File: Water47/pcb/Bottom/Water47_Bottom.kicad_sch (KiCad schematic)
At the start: 5 parts, among them U1 MOUDLE-SEEEDUINO-XIAO

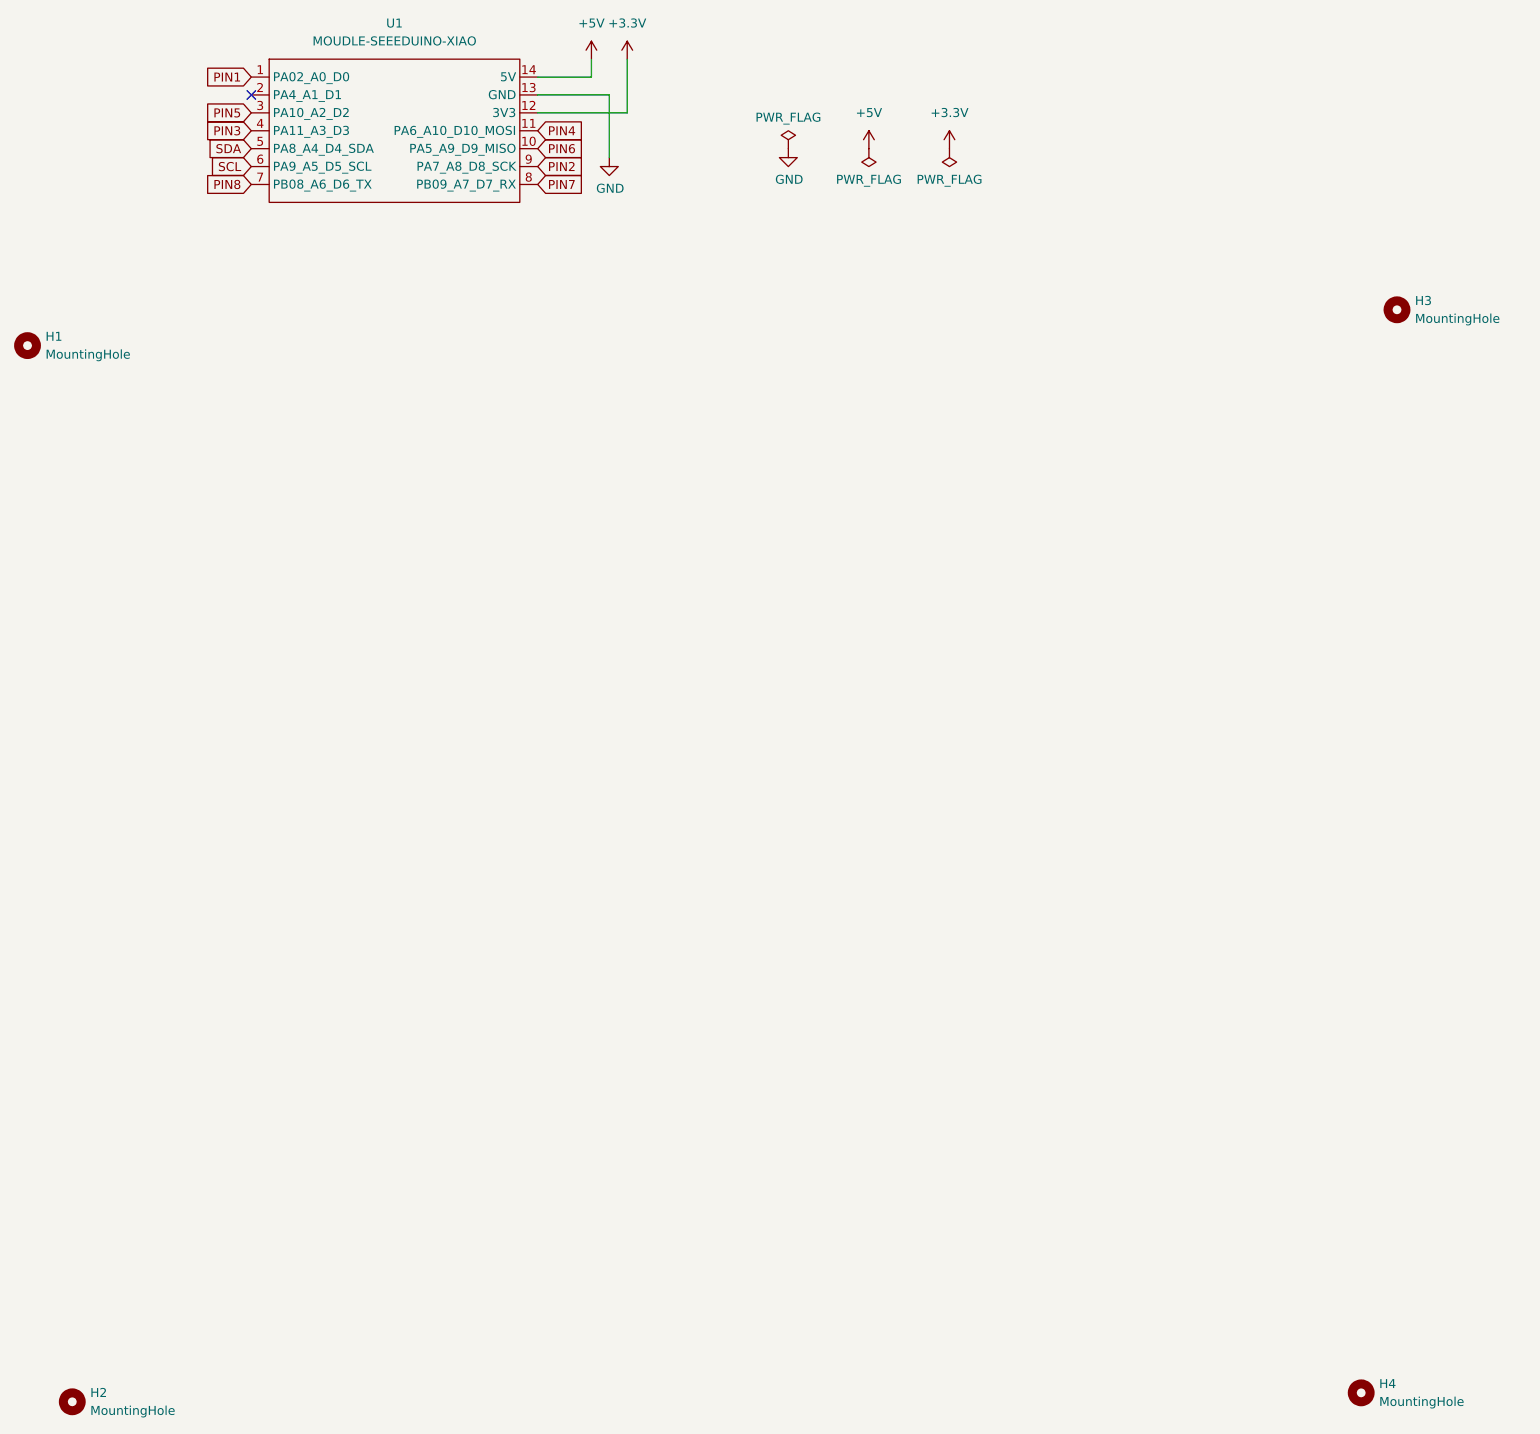
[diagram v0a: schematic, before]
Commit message: feat: add mounting holes
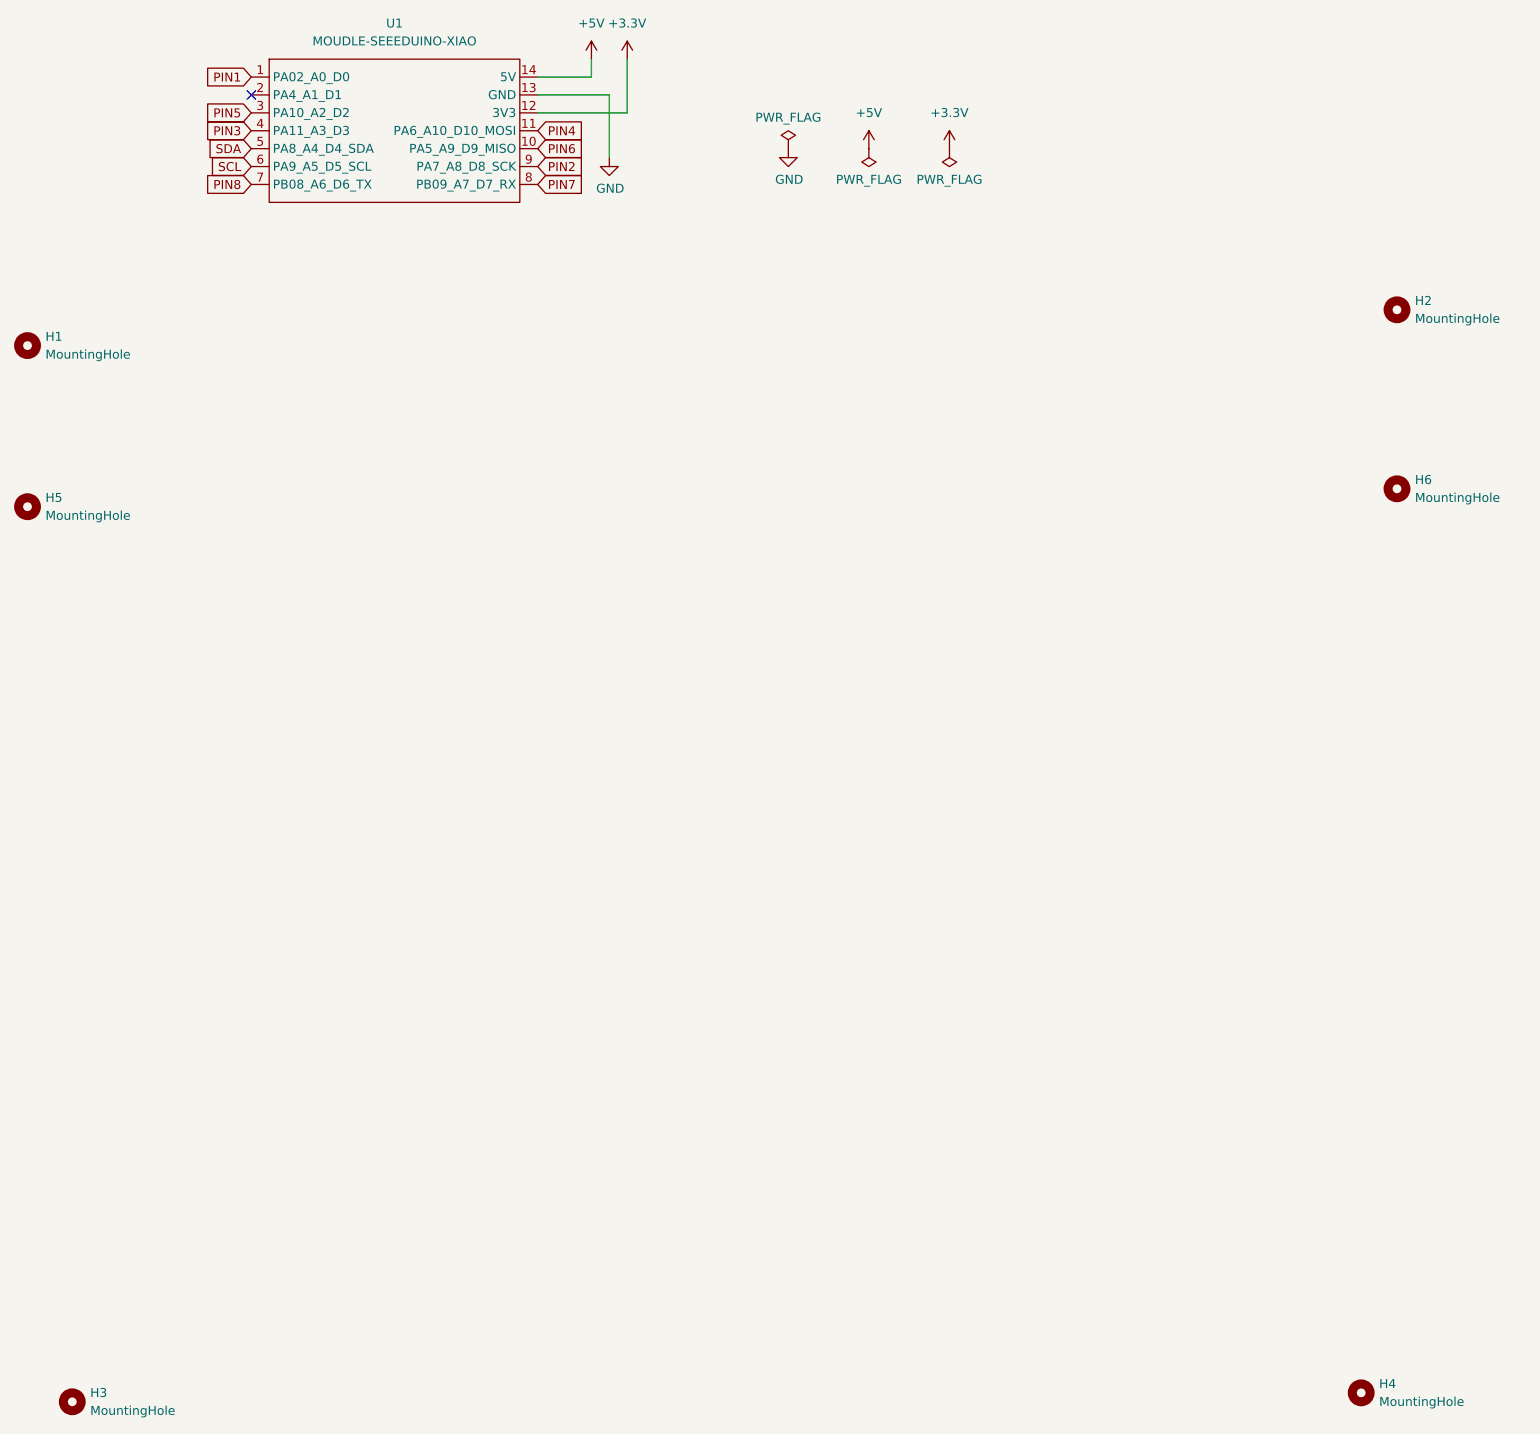
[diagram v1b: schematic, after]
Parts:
- added H5, H6: MountingHole, kbd_Hole:m2_Screw_Hole, symbol Mechanical:MountingHole
- renumbered H3 to H2, H2 to H3
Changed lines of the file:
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@@
+    )
+  )
+  (symbol (lib_id "Mechanical:MountingHole") (at 22.86 91.44 0) (unit 1)
+    (in_bom yes) (on_board yes) (fields_autoplaced)
+    (property "Reference" "H5" (id 0) (at 25.4 90.1699 0)
+      (effects (font (size 1.27 1.27)) (justify left))
+    )
+    (property "Value" "MountingHole" (id 1) (at 25.4 92.7099 0)
+      (effects (font (size 1.27 1.27)) (justify left))
+    )
+    (property "Footprint" "kbd_Hole:m2_Screw_Hole" (id 2) (at 22.86 91.44 0)
+      (effects (font (size 1.27 1.27)) hide)
+    )
+    (property "Datasheet" "~" (id 3) (at 22.86 91.44 0)
+      (effects (font (size 1.27 1.27)) hide)
     )
   )
@@
     (pin "1")
   )
+  (symbol (lib_id "Mechanical:MountingHole") (at 217.17 88.9 0) (unit 1)
+    (in_bom yes) (on_board yes) (fields_autoplaced)
+    (property "Reference" "H6" (id 0) (at 219.71 87.6299 0)
+      (effects (font (size 1.27 1.27)) (justify left))
+    )
+    (property "Value" "MountingHole" (id 1) (at 219.71 90.1699 0)
+      (effects (font (size 1.27 1.27)) (justify left))
+    )
+    (property "Footprint" "kbd_Hole:m2_Screw_Hole" (id 2) (at 217.17 88.9 0)
+      (effects (font (size 1.27 1.27)) hide)
+    )
+    (property "Datasheet" "~" (id 3) (at 217.17 88.9 0)
+      (effects (font (size 1.27 1.27)) hide)
+    )
+  )
   (symbol (lib_id "power:PWR_FLAG") (at 153.67 40.64 180) (unit 1)
     (in_bom yes) (on_board yes)
@@
   (symbol (lib_id "Mechanical:MountingHole") (at 29.21 218.44 0) (unit 1)
     (in_bom yes) (on_board yes) (fields_autoplaced)
-    (property "Reference" "H2" (id 0) (at 31.75 217.1699 0)
+    (property "Reference" "H3" (id 0) (at 31.75 217.1699 0)
       (effects (font (size 1.27 1.27)) (justify left))
     )
@@
   (symbol (lib_id "Mechanical:MountingHole") (at 217.17 63.5 0) (unit 1)
     (in_bom yes) (on_board yes) (fields_autoplaced)
-    (property "Reference" "H3" (id 0) (at 219.71 62.2299 0)
+    (property "Reference" "H2" (id 0) (at 219.71 62.2299 0)
       (effects (font (size 1.27 1.27)) (justify left))
     )
@@
       (reference "H1") (unit 1) (value "MountingHole") (footprint "kbd_Hole:m2_Screw_Hole")
     )
+    (path "/f64ccafc-8d73-4e0d-a0a9-52c38f87dc6c"
+      (reference "H2") (unit 1) (value "MountingHole") (footprint "kbd_Hole:m2_Screw_Hole")
+    )
     (path "/bbde9b31-2ca1-42cc-a23f-bd08fc375c76"
-      (reference "H2") (unit 1) (value "MountingHole") (footprint "kbd_Hole:m2_Screw_Hole")
-    )
-    (path "/f64ccafc-8d73-4e0d-a0a9-52c38f87dc6c"
       (reference "H3") (unit 1) (value "MountingHole") (footprint "kbd_Hole:m2_Screw_Hole")
     )
@@
       (reference "H4") (unit 1) (value "MountingHole") (footprint "kbd_Hole:m2_Screw_Hole")
     )
+    (path "/041a22fb-bd25-45a3-b2de-1d6f113e8c70"
+      (reference "H5") (unit 1) (value "MountingHole") (footprint "kbd_Hole:m2_Screw_Hole")
+    )
+    (path "/5baf0ae5-116d-4142-b157-7cb2ebe3f02d"
+      (reference "H6") (unit 1) (value "MountingHole") (footprint "kbd_Hole:m2_Screw_Hole")
+    )
     (path "/d703529e-35b6-4856-b4e1-4ebcffe81b73"
